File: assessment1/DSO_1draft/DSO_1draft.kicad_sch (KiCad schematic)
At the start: 99 parts, among them J1 USB_A, J2 Conn_Coaxial, J3 Conn_Coaxial, J4 Conn_Coaxial, J5 Conn_Coaxial, J6 Conn_ARM_JTAG_SWD_10, U1 ADG708BRUZ, U2 ADG708BRUZ, U3 STM32G431C6Tx

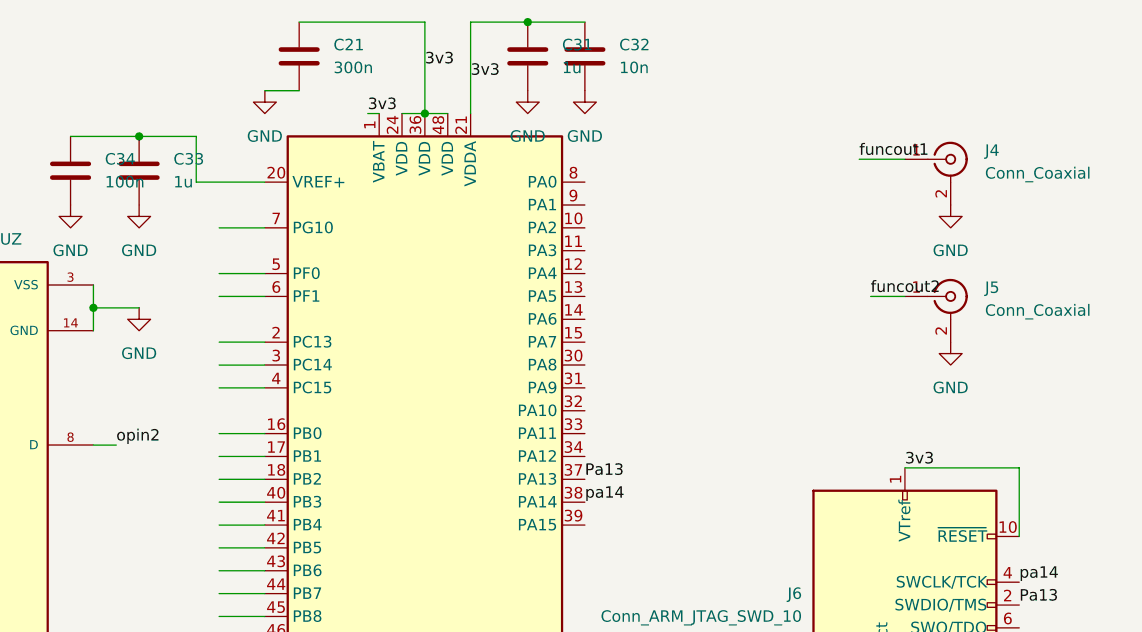
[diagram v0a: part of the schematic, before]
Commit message: updated schematics
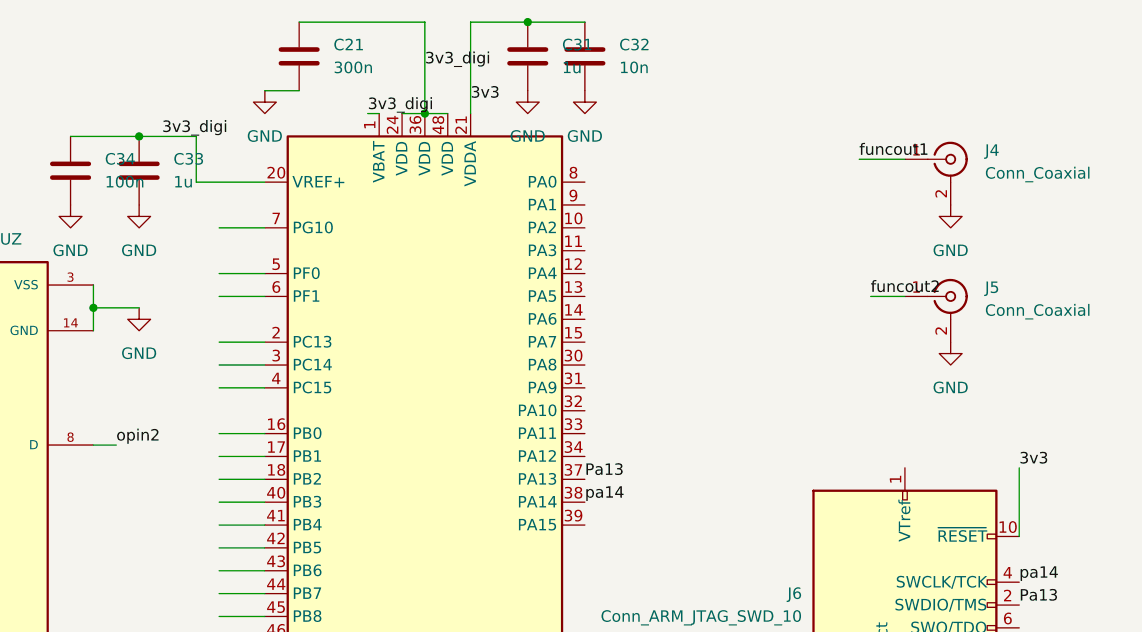
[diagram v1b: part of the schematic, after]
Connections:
- net 3v3: no longer C21.1, J6.1 (VTref), U3.1 (VBAT), U3.24 (VDD), U3.36 (VDD), U3.48 (VDD)
- net 3v3_digi: now also C21.1, C33.1, C34.1, U3.1 (VBAT), U3.20 (VREF+), U3.24 (VDD), U3.36 (VDD), U3.48 (VDD)
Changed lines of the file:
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@@
+	(wire
+		(pts
+			(xy 217.17 11.43) (xy 217.17 21.59)
+		)
+		(stroke
+			(width 0)
+			(type default)
+		)
+	)
 	(wire
 		(pts
@@
 	(wire
 		(pts
-			(xy 217.17 11.43) (xy 217.17 21.59)
-		)
-		(stroke
-			(width 0)
-			(type default)
-		)
-	)
-	(wire
-		(pts
 			(xy 232.41 124.46) (xy 240.03 124.46)
 		)
@@
 		(pts
 			(xy 213.36 128.27) (xy 213.36 130.81)
-		)
-		(stroke
-			(width 0)
-			(type default)
-		)
-	)
-	(wire
-		(pts
-			(xy 278.13 60.96) (xy 265.43 60.96)
 		)
 		(stroke
@@
 		)
 	)
+	(label "3v3_digi"
+		(at 182.88 24.13 0)
+		(effects
+			(font
+				(size 1.27 1.27)
+			)
+			(justify left bottom)
+		)
+	)
 	(label "pwmout1"
 		(at 62.23 130.81 0)
@@
 		)
 	)
-	(label "3v3"
+	(label "3v3_digi"
 		(at 205.74 21.59 0)
 		(effects
@@
 	)
 	(label "3v3"
-		(at 217.17 17.78 0)
+		(at 217.17 20.32 0)
 		(effects
 			(font
@@
 		)
 	)
-	(label "3v3"
+	(label "3v3_digi"
 		(at 212.09 16.51 0)
 		(effects
@@
 	)
 	(label "3v3"
-		(at 265.43 60.96 0)
-		(effects
-			(font
+		(at 278.13 60.96 0)
+		(effects
+			(font

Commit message: updated schematics
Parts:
- removed C25, C26: 10p, symbol Device:C
- removed L1: L_Ferrite_Small, symbol Device:L_Ferrite_Small
- removed R40, R41: R, symbol Device:R
- added D3, D4, D5, D6, D7, D8, D9: LED, symbol Device:LED
- added L1: 6.8u, symbol Device:L
- added R47, R48: 10k, symbol Device:R
- added R49: R, symbol Device:R
- added R50, R51, R52, R53, R54, R55: 1k, symbol Device:R
- added SW1: SW_SPDT, symbol Switch:SW_SPDT
- C1, C2: value C -> 4.7u
- C20, C22: value 10p -> 2.2p
- C3: value C -> 10u
- R14, R16: value 1k -> 10k
- R22, R23, R24, R25, R27, R33, R35: value R -> 1k
- R26, R28, R36: value R -> 2k
- R29, R37: value R -> 10k
- R31, R32: value R -> 1K
- R34: value R -> 2K
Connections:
- net OPA2out is gone; now on net PA2_OP1_OUT: R44.1
- net PB0+ is gone; now on net PA1_OP1+: C28.1, R43.2
- net opout3 is gone; now on net OP4_OUT: C23.2, probopamp1.8 (OUTC), probopamp1.9 (-INC)
- net pwm2 is gone; now on net PB3_TM2_2: R5.1
- net 3v3: now also C33.1, C34.1, U3.20 (VREF+); no longer J6.10 (~{RESET}), U1.13 (VDD), U2.13 (VDD)
- net 3v3_digi: now also J6.1 (VTref), R47.1; no longer C33.1, C34.1, U3.20 (VREF+)
- net 5v: now also U1.13 (VDD), U2.13 (VDD), R49.1; no longer C1.1, J1.1 (VBUS)
- net A0: now also U3.43 (PB6), R53.1
- net A1: now also U3.44 (PB7), R54.1
- net A2: now also U3.46 (PB9), R55.1
- net B0: now also U3.17 (PB1), R50.1
- net B1: now also U3.41 (PB4), R51.1
- net B2: now also U3.42 (PB5), R52.1
- net D+: now also U3.34 (PA12)
- net D-: now also U3.33 (PA11)
- net DAC1: now also U3.12 (PA4)
- net DAC2: now also U3.13 (PA5)
- net GND: now also D3.1 (K), D4.1 (K), D5.1 (K), D6.1 (K), D7.1 (K), D8.1 (K), D9.1 (K), R48.1
- net S1B: now also C20.1, R14.2, R30.1, probopamp1.6 (-INB); no longer R30.2, R31.1, U2.4 (S1)
- net S2B: now also R30.2, R31.1, U2.4 (S1); no longer R31.2, R32.1, U2.5 (S2)
- net S3B: now also R31.2, R32.1, U2.5 (S2); no longer R32.2, R33.1, U2.6 (S3)
- net S4B: now also R32.2, R33.1, U2.6 (S3); no longer R33.2, R34.1, U2.7 (S4)
- net S5B: now also R33.2, R34.1, U2.7 (S4); no longer R34.2, R35.1, U2.12 (S5)
- net S6B: now also R34.2, R35.1, U2.12 (S5); no longer R35.2, R36.1, U2.11 (S6)
- net S7B: now also R35.2, R36.1, U2.11 (S6); no longer R36.2, R37.1, U2.10 (S7)
- net opout1: now also R42.1; no longer R16.2
- net opout2: now also U2.8 (D); no longer R14.2, R15.1, R42.1
- net probA1: now also R16.1; no longer R22.1
- net probB1: now also R14.1; no longer R30.1
- net at C2.1, dcdciso1.2 (+VIN): now also L1.2
- net PA2_OP1_OUT: now reaches U3.10 (PA2)
- net PA2_OP1_OUT: now also C27.2
- net PA3_OP1-: now reaches U3.11 (PA3)
- net PA6_OP2_OUT: now reaches U3.14 (PA6)
- net PA6_OP2_OUT: now also R15.1
- net PB0_OP2+: now reaches U3.16 (PB0)
- net PA0_ADC_IN1: now reaches U3.18 (PB2)
- net PA0_ADC_IN1: now also C29.2, U3.8 (PA0)
- net PB10_TM2_3: now reaches U3.22 (PB10)
- net PB11_TM2_4: now reaches U3.25 (PB11)
- net PB13_OP3+: now reaches U3.27 (PB13)
- net PB13_OP3+: now also C30.1, R45.2
- net OP4_OUT: now reaches U3.29 (PB15)
- net PA15_TM2_1: now reaches U3.39 (PA15)
- net PB3_TM2_2: now reaches U3.40 (PB3)
- net at U3.45 (PB8): now also R48.2
- net PG10_NRST: now reaches U3.7 (PG10)
- net PG10_NRST: now also J6.10 (~{RESET}), R47.2
- net PA1_OP1+: now reaches U3.9 (PA1)
- net Pa13 renamed PA13_SWDIO
- removed net opA6out: C27.2, C29.2, C30.1, R45.2
- net opin1 renamed S0
- net S0: now also R16.2, R22.1; no longer R16.1
- removed net opin2: C20.1, R14.1, U2.8 (D), probopamp1.6 (-INB)
- net opin3+ renamed OP4_IN+
- net pa14 renamed PA14_SCLK
- net pwm1 renamed PB3_TM2_1
- net pwm3 renamed PB3_TM2_3
- net pwm4 renamed PB3_TM2_4
- net pwmin3 renamed pwmopout3
- net pwmopout3: now also pwmoppamp1.12 (IN4+); no longer pwmoppamp1.10 (IN3+)
- net pwmin4 renamed pwmopout4
- net pwmopout4: now also pwmoppamp1.10 (IN3+); no longer pwmoppamp1.12 (IN4+)
- new net: D9.2 (A), R55.2
- new net: D8.2 (A), R54.2
- new net: D6.2 (A), R52.2
- new net: D3.2 (A), R49.2
- new net: J1.1 (VBUS), SW1.2 (B)
- new net: D5.2 (A), R51.2
- new net: D4.2 (A), R50.2
- new net: D7.2 (A), R53.2
- new net 5V: C1.1, L1.1, SW1.1 (A)
- new net S8B: R36.2, R37.1, U2.10 (S7)
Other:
- note added: "ANTI ALIASING TO INTERNAL ADC CONN"
- note added: "Attenuator network to OPamp conn"
- note added: "D+ AND D- CONN"
- note added: "DAC out from mcu & DAC in to OPamp conn"
- note added: "PWM inputs to OPamps & Timers output from mcu conn"
- note added: "SELECT PIN MCU & ANALOG MUX CONN"
- moved on the sheet: C1, C10, C11, C12, C13, C14, C15, C16, C17, C18, C19, C2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

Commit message: some footprints assigned
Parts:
- added C25, C26: 10p, symbol Device:C
- added J8: Conn_01x20, symbol Connector_Generic:Conn_01x20
- added R40, R41: R, symbol Device:R
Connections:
- net 5V is gone; now on net 5v: C1.1, L1.1, SW1.1 (A)
- net -5v: now also J8.19 (Pin_19)
- net 3v3_digi: now also J8.18 (Pin_18)
- net 5v: now also J8.17 (Pin_17)
- net GND: now also C26.2, J8.20 (Pin_20)
- net PA6_OP2_OUT: now also C25.2
- net PB0_OP2+: now also C26.1, R41.2
- net PG10_NRST: now also J8.16 (Pin_16)
- net opout2: now also R40.1
- net PB8: now reaches R48.2, U3.45 (PB8)
- net PB8: now also J8.15 (Pin_15)
- net PA7: now reaches U3.15 (PA7)
- net PA7: now also J8.8 (Pin_8)
- net PC13: now reaches U3.2 (PC13)
- net PC13: now also J8.3 (Pin_3)
- net PB12: now reaches U3.26 (PB12)
- net PB12: now also J8.6 (Pin_6)
- net PB14: now reaches U3.28 (PB14)
- net PB14: now also J8.7 (Pin_7)
- net PC14: now reaches U3.3 (PC14)
- net PC14: now also J8.4 (Pin_4)
- net PA8: now reaches U3.30 (PA8)
- net PA8: now also J8.9 (Pin_9)
- net PA9: now reaches U3.31 (PA9)
- net PA9: now also J8.10 (Pin_10)
- net PA10: now reaches U3.32 (PA10)
- net PA10: now also J8.11 (Pin_11)
- net PC15: now reaches U3.4 (PC15)
- net PC15: now also J8.5 (Pin_5)
- net PF0: now reaches U3.5 (PF0)
- net PF0: now also J8.1 (Pin_1)
- net PF1: now reaches U3.6 (PF1)
- net PF1: now also J8.2 (Pin_2)
- net EOP+: now reaches probopamp1.12 (+IND)
- net EOP+: now also J8.12 (Pin_12)
- net EOP-: now reaches probopamp1.13 (-IND)
- net EOP-: now also J8.13 (Pin_13)
- net EOP_OUT: now reaches probopamp1.14 (OUTD)
- net EOP_OUT: now also J8.14 (Pin_14)
- new net: C25.1, R40.2, R41.1
- no-connect marks 0 -> 4
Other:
- moved on the sheet: C20, R14

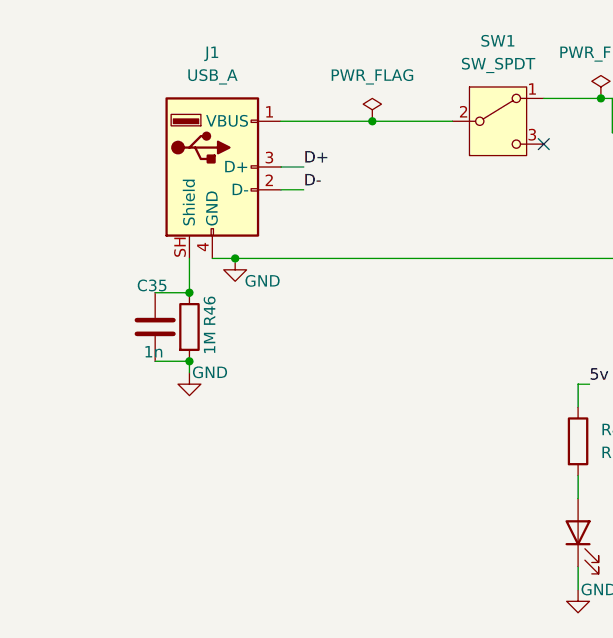
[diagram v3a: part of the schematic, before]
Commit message: upadted to add stacked USB
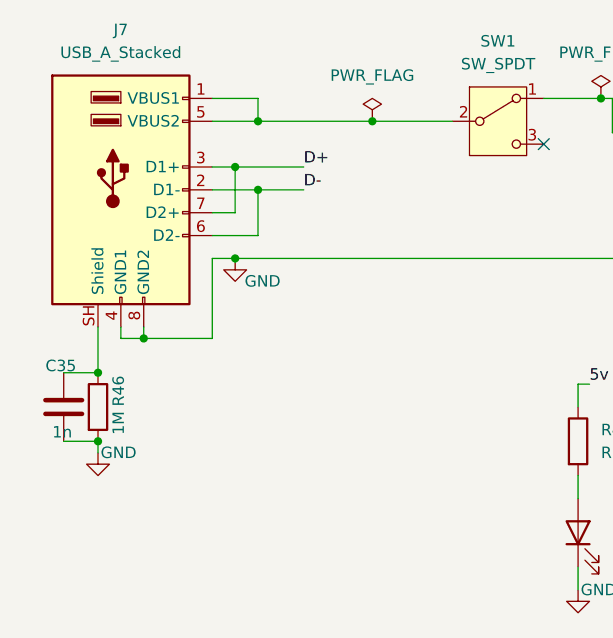
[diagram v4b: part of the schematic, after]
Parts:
- removed J1: USB_A, symbol Connector:USB_A
- added J7: USB_A_Stacked, symbol Connector:USB_A_Stacked
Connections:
- net D+: now also J7.3 (D1+), J7.7 (D2+)
- net D-: now also J7.2 (D1-), J7.6 (D2-)
- net GND: now also J7.4 (GND1), J7.8 (GND2)
- net at C35.1, R46.1: now also J7.SH (Shield)
- net at SW1.2 (B): now also J7.1 (VBUS1), J7.5 (VBUS2)
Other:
- moved on the sheet: C35, R46

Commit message: modifid circuit according to parts avavailable
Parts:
- removed J6: Conn_ARM_JTAG_SWD_10, symbol Connector:Conn_ARM_JTAG_SWD_10
- removed R2: 71.5k, symbol Device:R
- added C36, C37, C38, C39: 1n, Capacitor_SMD:C_0805_2012Metric_Pad1.18x1.45mm_HandSolder, symbol Device:C
- added C40, C41: 100n, Capacitor_SMD:C_0805_2012Metric_Pad1.18x1.45mm_HandSolder, symbol Device:C
- added J1: Conn_01x05, Connector_PinHeader_2.54mm:PinHeader_1x05_P2.54mm_Vertical, symbol Connector_Generic:Conn_01x05
- added J9: Conn_01x20, Connector_PinHeader_2.54mm:PinHeader_2x10_P2.54mm_Vertical, symbol Connector_Generic:Conn_01x20
- added R56: 10k, Resistor_SMD:R_0805_2012Metric_Pad1.20x1.40mm_HandSolder, symbol Device:R
- added SW2: SW_SPDT, Slide_switch:SS-12F17_1P2T, symbol Switch:SW_SPDT
- C1, C10, C12, C15, C18, C2, C20, C22, C3, C31, C32, C33, C34, C35, C4, C5, C6, C7: footprint (none) -> Capacitor_SMD:C_0805_2012Metric_Pad1.18x1.45mm_HandSolder
- C11, C14, C17, C8: value 47n -> 1n; footprint (none) -> Capacitor_SMD:C_0805_2012Metric_Pad1.18x1.45mm_HandSolder
- C13, C16, C19, C9: value 5.6n -> 1n; footprint (none) -> Capacitor_SMD:C_0805_2012Metric_Pad1.18x1.45mm_HandSolder
- C21: value 300n -> 100n; footprint (none) -> Capacitor_SMD:C_0805_2012Metric_Pad1.18x1.45mm_HandSolder
- C23, C29: value 10p -> 820p; footprint (none) -> Capacitor_SMD:C_0805_2012Metric_Pad1.18x1.45mm_HandSolder
- C24, C25, C26, C27, C28, C30: value 10p -> 100p; footprint (none) -> Capacitor_SMD:C_0805_2012Metric_Pad1.18x1.45mm_HandSolder
- D1, D2: footprint P6KE13CA:DIOAD1300W80L670D310 -> TVSdiode:DIOAD1300W80L670D310
- D3, D4, D5, D6, D7, D8, D9: footprint (none) -> LED_SMD:LED_1206_3216Metric
- J2, J3, J4, J5: footprint (none) -> Connector_Coaxial:BNC_Amphenol_B6252HB-NPP3G-50_Horizontal
- J7: footprint (none) -> Connector_USB:USB_A_CUI_UJ2-ADH-TH_Horizontal_Stacked
- J8: footprint (none) -> Connector_PinHeader_2.54mm:PinHeader_2x10_P2.54mm_Vertical
- L1: footprint (none) -> Inductor_THT:L_Axial_L11.0mm_D4.5mm_P15.24mm_Horizontal_Fastron_MECC
- R1: value R -> 100; footprint (none) -> Resistor_THT:R_Axial_DIN0207_L6.3mm_D2.5mm_P7.62mm_Horizontal
- R10, R13, R7: value 71.5k -> 10k; footprint (none) -> Resistor_SMD:R_0805_2012Metric_Pad1.20x1.40mm_HandSolder
- R11, R4, R5, R8: value 4.42k -> 10k; footprint (none) -> Resistor_SMD:R_0805_2012Metric_Pad1.20x1.40mm_HandSolder
- R12, R3, R6, R9: value 56.2k -> 10k; footprint (none) -> Resistor_SMD:R_0805_2012Metric_Pad1.20x1.40mm_HandSolder
- R14, R16, R17, R18, R19, R20, R22, R23, R24, R25, R26, R27, R28, R29, R30, R31, R32, R33, R34, R35, R36, R37, R38, R39, R47, R48, R50, R51, R52, R53, R54, R55: footprint (none) -> Resistor_SMD:R_0805_2012Metric_Pad1.20x1.40mm_HandSolder
- R15, R21, R44, R45, R49: value R -> 1k; footprint (none) -> Resistor_SMD:R_0805_2012Metric_Pad1.20x1.40mm_HandSolder
- R40, R41, R42, R43: value R -> 2k; footprint (none) -> Resistor_SMD:R_0805_2012Metric_Pad1.20x1.40mm_HandSolder
- R46: footprint (none) -> Resistor_THT:R_Axial_DIN0207_L6.3mm_D2.5mm_P7.62mm_Horizontal
- SW1: footprint (none) -> Slide_switch:SS-12F17_1P2T
- U1, U2: footprint ADG708BRUZ:TSSOP16 -> Analog_mux:TSSOP16
- anlgLDO1: footprint LP5907MFX-3.3_NOPB:SOT95P280X145-5N -> analogLDO:SOT95P280X145-5N
- dcdciso1: footprint RO-053.3S_HP:CONV_RO-053.3S_HP -> DCDCisolator:CONV_RO-053.3S_HP
- digildo1: footprint AMS1117-3.3:SOT229P700X180-4N -> digiLDO:SOT229P700X180-4N
- funcopamp1: footprint NE5532DR:SOIC127P599X175-8N -> FuncOPAMP:SOIC127P599X175-8N
- probopamp1: footprint TLV9064IPWT:SOP65P640X120-14N -> probingopamp:SOP65P640X120-14N
- pwmoppamp1: footprint U_TSSOP_PW_TEX -> pwmopamp:U_TSSOP_PW_TEX-M
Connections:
- net 3v3: now also SW2.1 (A)
- net 3v3_digi: now also C40.1, C41.1, J1.1 (Pin_1), R56.1; no longer R47.1
- net 5v: now also SW2.3 (C); no longer U1.13 (VDD), U2.13 (VDD)
- net A0: now also J9.12 (Pin_12)
- net A1: now also J9.13 (Pin_13)
- net A2: now also J9.14 (Pin_14)
- net B0: now also J9.9 (Pin_9)
- net B1: now also J9.10 (Pin_10)
- net B2: now also J9.11 (Pin_11)
- net D+: now also J9.16 (Pin_16)
- net D-: now also J9.15 (Pin_15)
- net DAC1: now also J9.7 (Pin_7)
- net DAC2: now also J9.8 (Pin_8)
- net GND: now also C12.2, C15.2, C18.2, C40.2, C41.2, J1.5 (Pin_5); no longer C13.2, C16.2, C19.2
- net OP4_OUT: now also J9.2 (Pin_2)
- net PA0_ADC_IN1: now also J9.1 (Pin_1)
- net PA13_SWDIO: now also J1.4 (Pin_4)
- net PA14_SCLK: now also J1.3 (Pin_3)
- net PB3_TM2_1: now also J9.3 (Pin_3)
- net PB3_TM2_2: now also J9.4 (Pin_4)
- net PB3_TM2_3: now also J9.5 (Pin_5)
- net PB3_TM2_4: now also J9.6 (Pin_6)
- net PG10_NRST: now also J1.2 (Pin_2), R56.2; no longer R47.2
- net S0: now also J9.18 (Pin_18)
- net S1B: now also J9.17 (Pin_17)
- net pwmopout3: now also C15.1; no longer C16.1
- net pwmopout4: now also C18.1; no longer C19.1
- net pwmout1: now also C36.2
- net pwmout2: now also C13.2, C37.2; no longer C12.2
- net pwmout3: now also C16.2, C38.2; no longer C15.2
- net pwmout4: now also C19.2, C39.2; no longer C18.2
- net at R10.1, R9.2: now also C16.1, C38.1; no longer C15.1
- net at R6.2, R7.1: now also C13.1, C37.1; no longer C12.1
- net at R12.2, R13.1: now also C19.1, C39.1; no longer C18.1
- net at C9.1, pwmoppamp1.3 (IN1+): now also R47.2
- net at R7.2, pwmoppamp1.5 (IN2+): now also C12.1; no longer C13.1
- net at C10.1, R3.2: now also R47.1, C36.1
- new net SelSupp: SW2.2 (B), U1.13 (VDD), U2.13 (VDD)
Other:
- note added: "This stage contains conn. to ST-Link"

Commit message: modified circuit A/C to new BOM
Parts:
- added C42: 100n, Capacitor_SMD:C_1206_3216Metric_Pad1.33x1.80mm_HandSolder, symbol Device:C
- added C44: 47u, Capacitor_THT:C_Radial_D5.0mm_H11.0mm_P2.00mm, symbol Device:C_Polarized
- C1, C10, C11, C12, C13, C14, C15, C16, C17, C18, C19, C2, C21, C24, C25, C26, C27, C28, C3, C30, C31, C32, C33, C34, C35, C36, C37, C38, C39, C4, C40, C41, C5, C6, C7, C8, C9: footprint Capacitor_SMD:C_0805_2012Metric_Pad1.18x1.45mm_HandSolder -> Capacitor_SMD:C_1206_3216Metric_Pad1.33x1.80mm_HandSolder
- C20, C22: value 2.2p -> 10p; footprint Capacitor_SMD:C_0805_2012Metric_Pad1.18x1.45mm_HandSolder -> Capacitor_SMD:C_1206_3216Metric_Pad1.33x1.80mm_HandSolder
- C23, C29: value 820p -> 680p; footprint Capacitor_SMD:C_0805_2012Metric_Pad1.18x1.45mm_HandSolder -> Capacitor_SMD:C_1206_3216Metric_Pad1.33x1.80mm_HandSolder
- R10, R11, R12, R13, R14, R15, R16, R17, R18, R19, R20, R21, R22, R23, R24, R25, R27, R29, R3, R30, R31, R32, R33, R35, R37, R38, R39, R4, R44, R45, R47, R48, R49, R5, R50, R51, R52, R53, R54, R55, R56, R6, R7, R8, R9: footprint Resistor_SMD:R_0805_2012Metric_Pad1.20x1.40mm_HandSolder -> Resistor_SMD:R_1206_3216Metric_Pad1.30x1.75mm_HandSolder
- R26, R28, R36, R40, R41, R42, R43: value 2k -> 2.2k; footprint Resistor_SMD:R_0805_2012Metric_Pad1.20x1.40mm_HandSolder -> Resistor_SMD:R_1206_3216Metric_Pad1.30x1.75mm_HandSolder
- R34: value 2K -> 2.2k; footprint Resistor_SMD:R_0805_2012Metric_Pad1.20x1.40mm_HandSolder -> Resistor_SMD:R_1206_3216Metric_Pad1.30x1.75mm_HandSolder
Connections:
- net 5v: now also C42.1, C44.1
- net GND: now also C42.2, C44.2

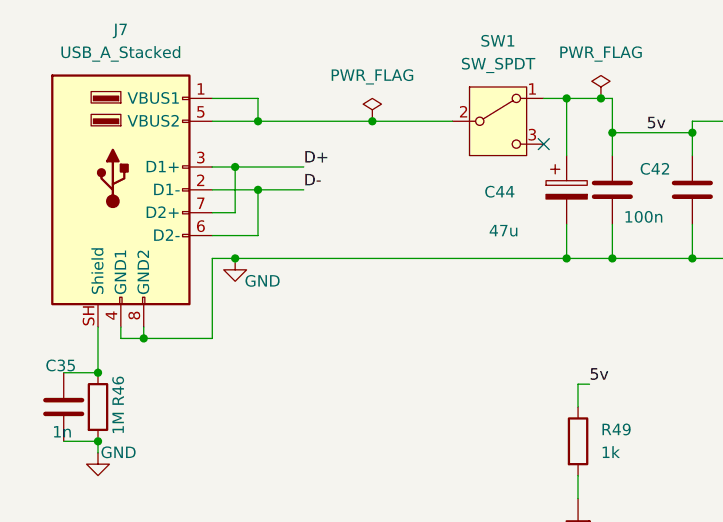
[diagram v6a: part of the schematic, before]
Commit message: added switch for usb_stack
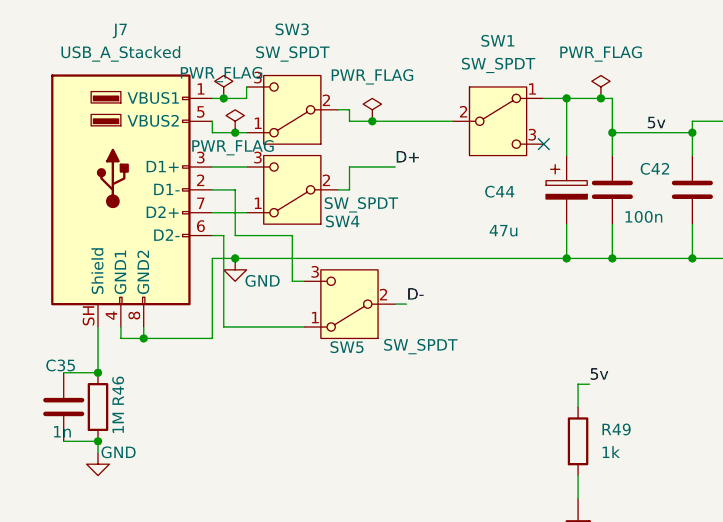
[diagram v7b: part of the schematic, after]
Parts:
- added SW3, SW4, SW5: SW_SPDT, Slide_switch:SS-12F17_1P2T, symbol Switch:SW_SPDT
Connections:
- net D+: now also SW4.2 (B); no longer J7.3 (D1+), J7.7 (D2+)
- net D-: now also SW5.2 (B); no longer J7.2 (D1-), J7.6 (D2-)
- new net: J7.7 (D2+), SW4.1 (A)
- new net: J7.3 (D1+), SW4.3 (C)
- new net: J7.6 (D2-), SW5.1 (A)
- new net: J7.2 (D1-), SW5.3 (C)
- new net: J7.5 (VBUS2), SW3.1 (A)
- new net: SW1.2 (B), SW3.2 (B)
- new net: J7.1 (VBUS1), SW3.3 (C)
